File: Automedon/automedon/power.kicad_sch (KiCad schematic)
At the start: 27 parts, among them J29 3211771, J30 3211771, J31 3211771, J32 3211771, J33 3211771, J34 3211771, J35 3211771, J36 3211771, J37 3211771, J38 3211771, J39 3211771, J40 3211771, J41 3211771, J42 3211771, J43 3211771, J44 3211771, J46 3211771, J47 3211771, J48 3211771, J49 3211771, J5 3211771, J6 3211771

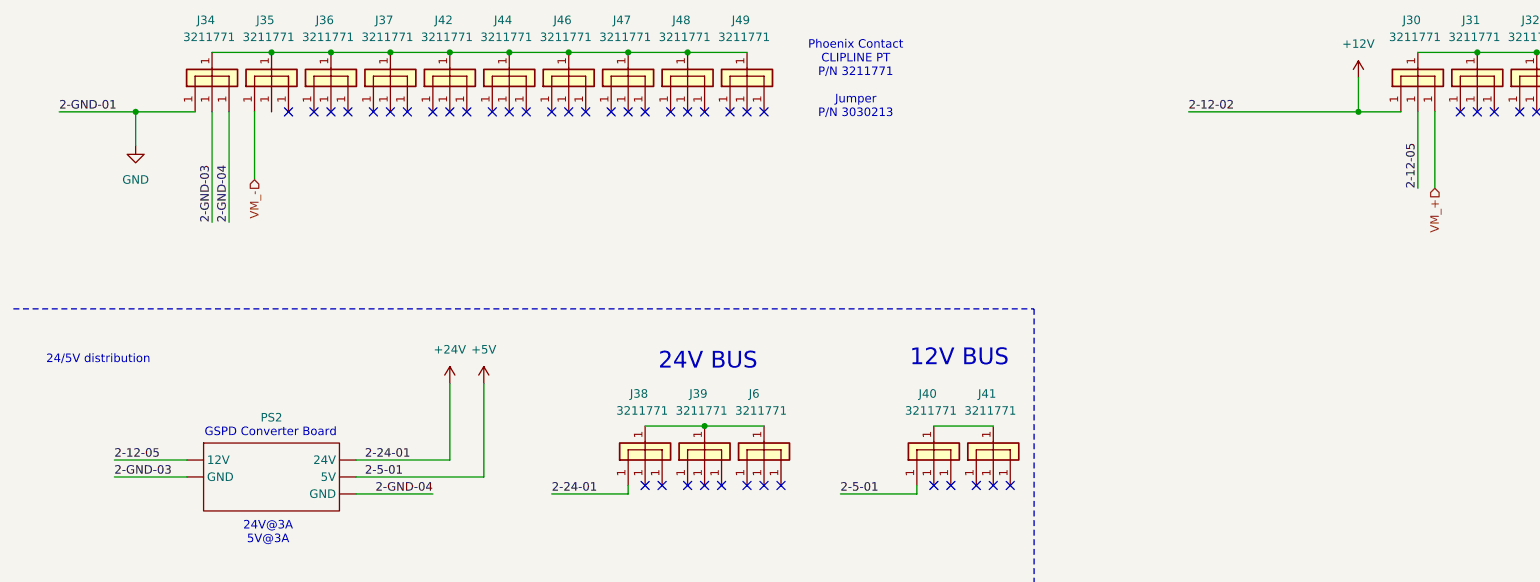
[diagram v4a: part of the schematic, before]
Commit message: Relabel 12V
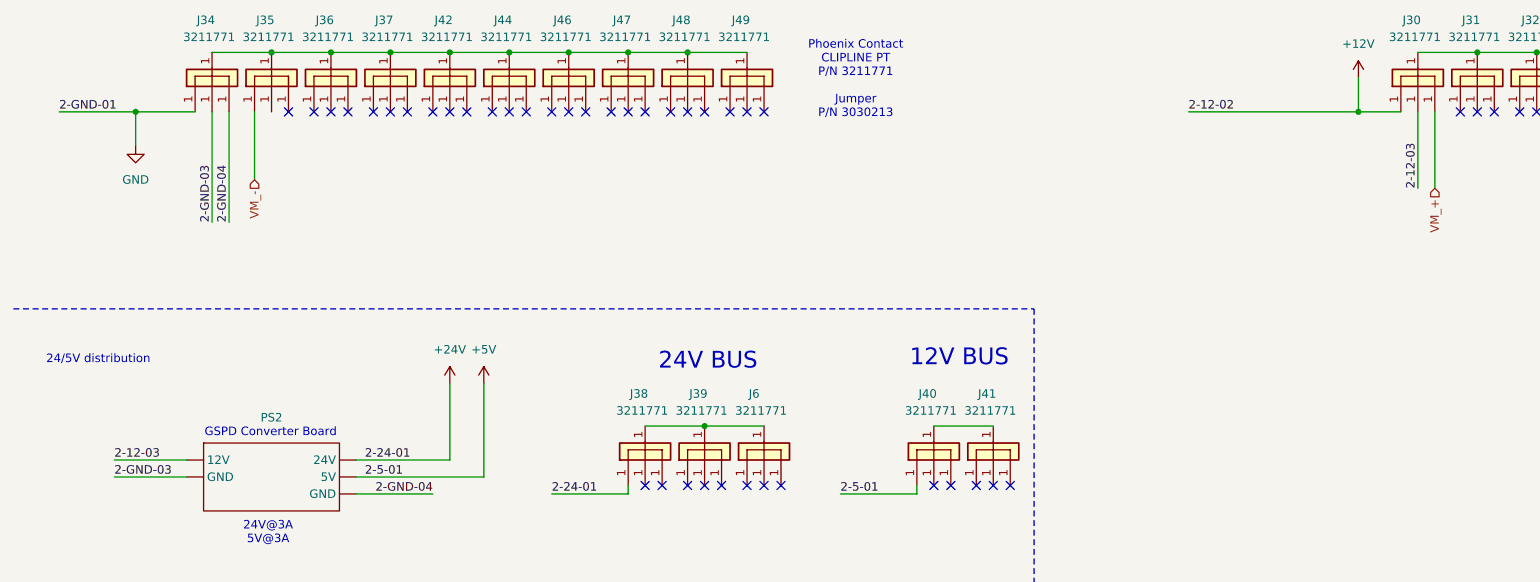
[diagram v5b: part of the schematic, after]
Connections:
- net at J37.1: now also J34.1, J35.1, J36.1, J42.1, J44.1, J46.1, J47.1, J48.1, J49.1
- net at J41.1: now also J40.1
- removed net 2-12-05: J30.1, PS2. (GND)
- new net: J30.1, J31.1, J32.1, J33.1, J43.1
- new net: J38.1, J39.1, J6.1
- new net 2-12-03: J30.1, PS2. (GND)
- now unconnected: J31.1, J32.1, J33.1, J36.1, J39.1, J42.1, J43.1, J44.1, J46.1, J47.1, J48.1, J49.1, J6.1
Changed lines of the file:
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@@
 		)
 	)
-	(label "2-12-05"
+	(label "2-12-03"
 		(at 222.25 129.54 90)
 		(effects
@@
 		)
 	)
-	(label "2-12-05"
+	(label "2-12-03"
 		(at 27.305 170.18 0)
 		(effects

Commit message: Update a bunch of shit
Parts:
- added J13, J16: 3211771, symbol automedon:CONN_TERM_3
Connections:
- net BATT1+: now also J16.1; no longer UPS1. (DC_IN_(+))
- net BATT1-: now also J13.1; no longer UPS1. (DC_IN_(+))
- net at J37.1: now also J34.1, J35.1, J36.1, J42.1, J44.1, J46.1, J47.1, J48.1, J49.1
- net at J41.1: now also J40.1
- new net: J30.1, J31.1, J32.1, J33.1, J43.1
- new net: J16.1, UPS1. (DC_IN_(+))
- new net: J13.1, UPS1. (DC_IN_(+))
- new net: J38.1, J39.1, J6.1
- new net BATT2+: J16.1
- new net BATT2-: J13.1
- now unconnected: J31.1, J32.1, J33.1, J36.1, J39.1, J42.1, J43.1, J44.1, J46.1, J47.1, J48.1, J49.1, J6.1
- no-connect marks 62 -> 64
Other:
- note added: "24V@3A 5V@3A ~8A in @ 12V"
- note added: "30A @ 12V"
- note added: "30A @ 12V max"
- note removed: "24V@3A 5V@3A"
- moved on the sheet: F1, UPS1
